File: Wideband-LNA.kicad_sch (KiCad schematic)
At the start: 30 parts, among them J1 RF-IN, J2 RF-OUT, J3 USB_C_Receptacle_USB2.0_16P, U1 TQP3M9036, U2 AP2127K-ADJ

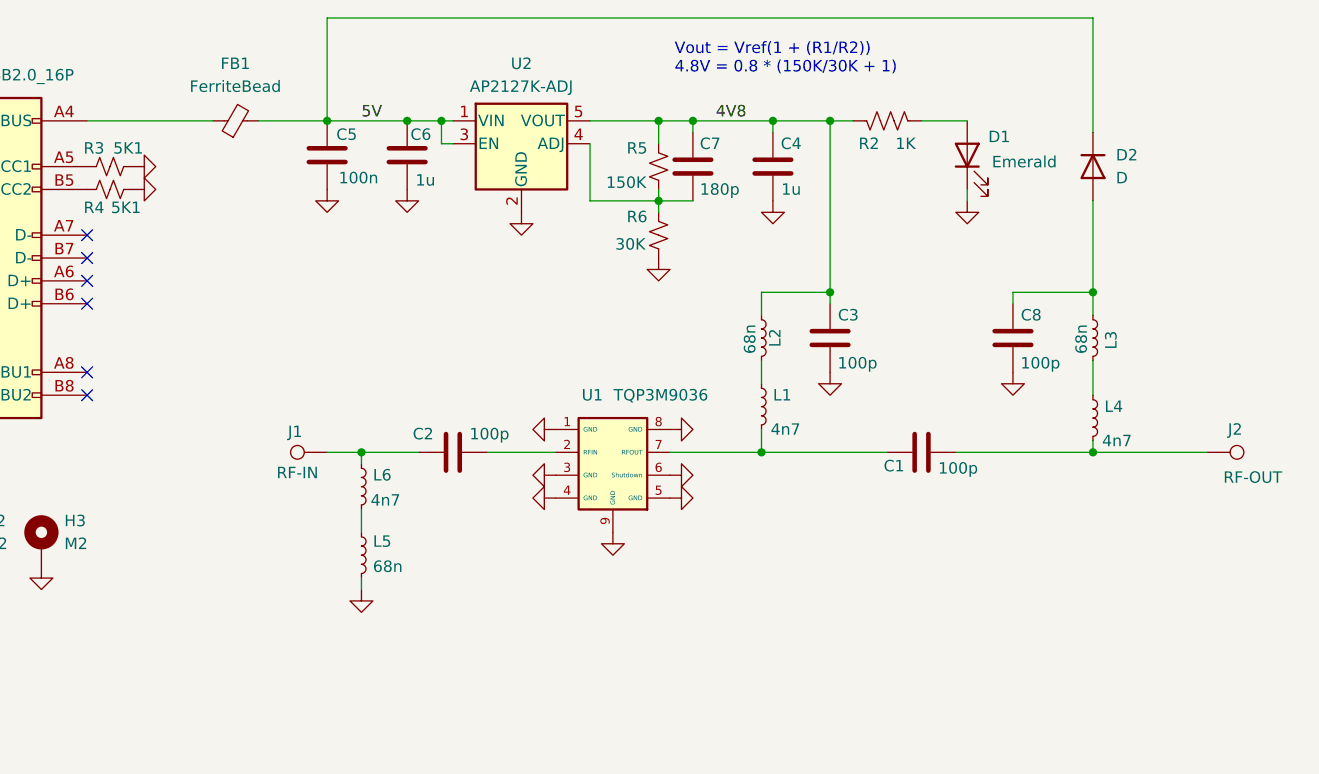
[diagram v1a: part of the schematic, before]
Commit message: updated design to match input at 144 MHz based on uSimmics modeling added 10 ohm resistor in power lead per suggestion from ZMS
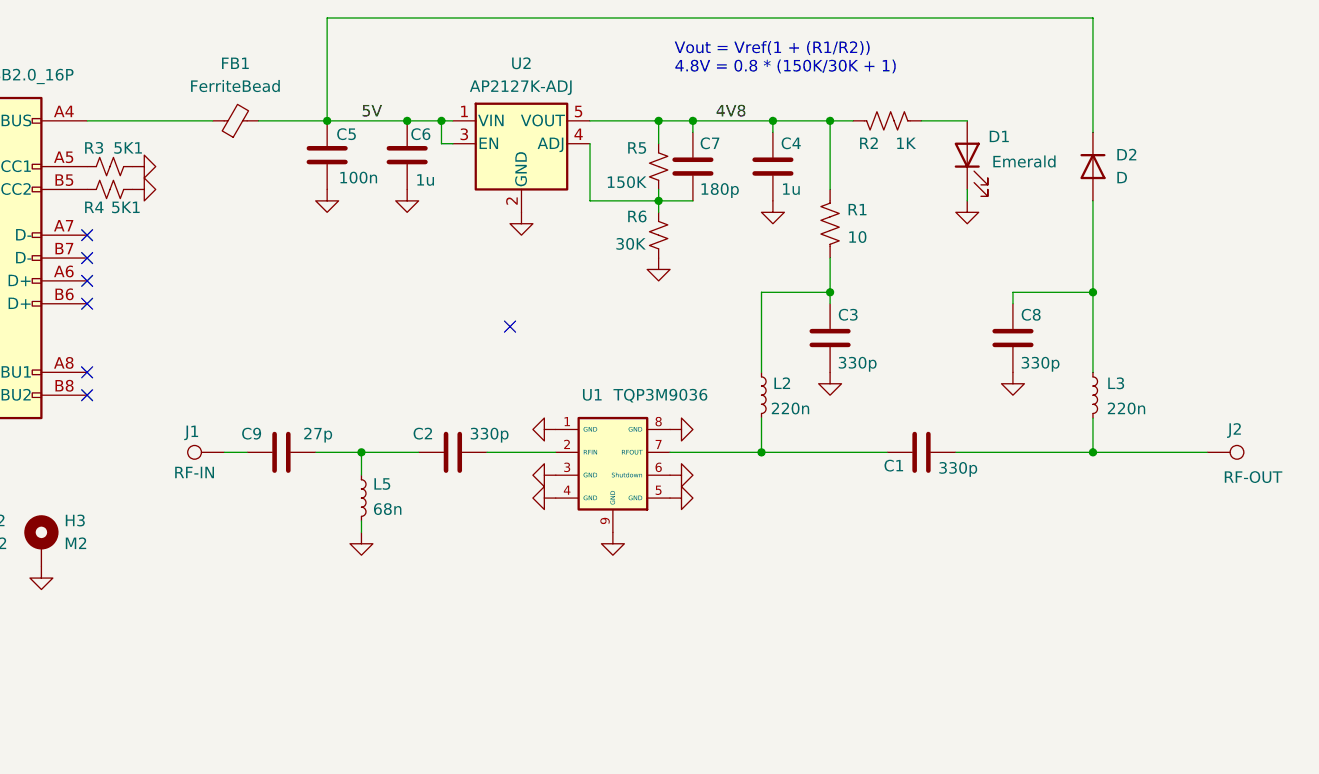
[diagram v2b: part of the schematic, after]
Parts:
- removed L1, L4, L6: 4n7, Inductor_SMD:L_0402_1005Metric, symbol Device:L_Small
- added C9: 27p, Capacitor_SMD:C_0402_1005Metric, symbol Device:C
- added R1: 10, Resistor_SMD:R_0402_1005Metric, symbol Device:R_US
- C1, C2, C3, C8: value 100p -> 330p
- L2, L3: value 68n -> 220n
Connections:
- net 4V8: now also R1.1; no longer C3.1, L2.1
- net at L2.2: now also C1.1, U1.7 (RFOUT)
- net at C1.2, J2.1: now also L3.2
- net at C2.1: now also L5.1, C9.2; no longer J1.1
- new net: C3.1, L2.1, R1.2
- new net: C9.1, J1.1
- no-connect marks 6 -> 7
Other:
- moved on the sheet: J1, L2, L3, L5

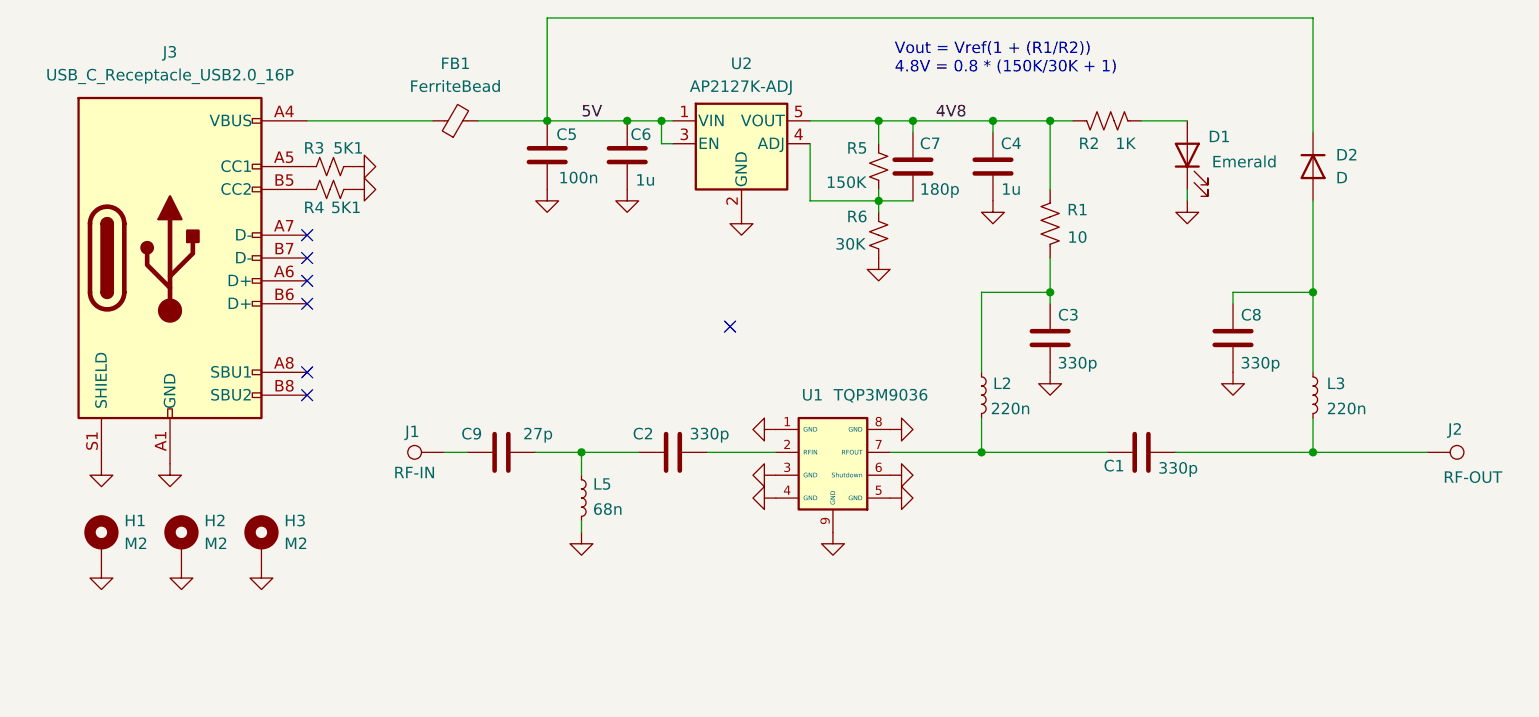
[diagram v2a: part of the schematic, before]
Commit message: Update layout to 19x19 enclosure, TQP3M9036 Improved ground via to isolate voltage regulator circuit from input goal of improving stability Add solder mask relief near output to improve contact with enclosure
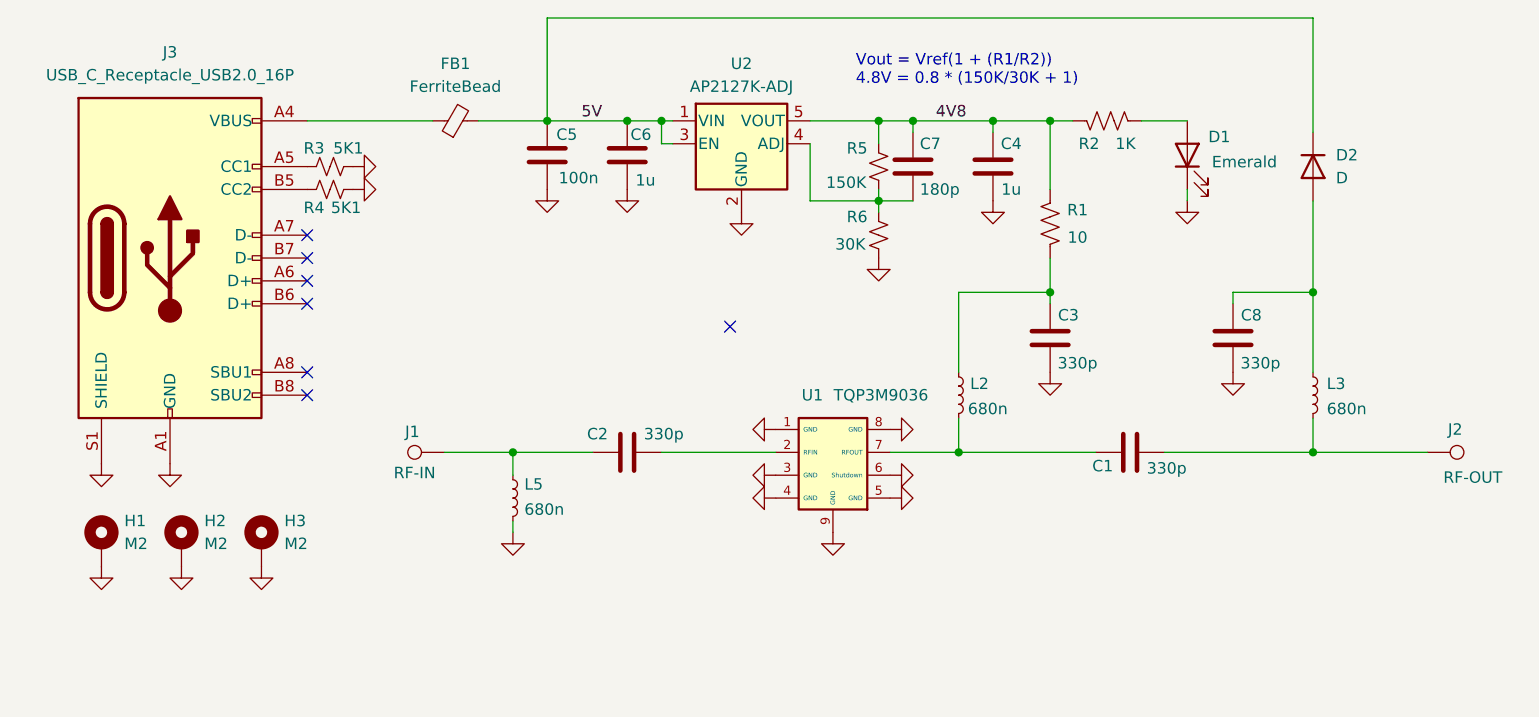
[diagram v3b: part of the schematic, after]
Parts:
- removed C9: 27p, Capacitor_SMD:C_0402_1005Metric, symbol Device:C
- D2: footprint Diode_SMD:D_SOD-123F -> Diode_SMD:D_SOD-523
- L2, L3: value 220n -> 680n
- L5: value 68n -> 680n
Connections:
- net at C2.1, L5.1: now also J1.1
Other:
- moved on the sheet: C1, C2, L2, L5

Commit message: Updated sheet titles to show Version and Git Branch
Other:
- note added: "Git Branch TQP3M9036_19x19_V3.4"
- note added: "November, 2025"
- note added: "Qorvo TQP3M9036 LNA 50 to 1500 MHz"
- note added: "V3.4"
- note removed: "January, 2025"
- note removed: "Qorvo TQP3M9037 LNA 0.5 dB NF, 18 dB gain, 33 dB OIP3, 500 to 6 GHz"
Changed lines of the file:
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@@
 	(generator_version "9.0")
 	(paper "USLetter")
+	(text "Git Branch TQP3M9036_19x19_V3.4"
+		(exclude_from_sim no)
+		(at 209.042 185.928 0)
+		(effects
+			(font
+				(size 1.27 1.27)
+			)
+		)
+	)
 	(text "V1\n"
 		(exclude_from_sim no)
@@
 		)
 	)
-	(text "January, 2025"
+	(text "November, 2025"
 		(exclude_from_sim no)
-		(at 214.122 193.294 0)
+		(at 198.374 199.136 0)
+		(effects
+			(font
+				(size 1.27 1.27)
+			)
+		)
+	)
+	(text "V3.4"
+		(exclude_from_sim no)
+		(at 253.492 199.39 0)
 		(effects
 			(font
@@
 		)
 	)
-	(text "Qorvo TQP3M9037 LNA 0.5 dB NF, 18 dB gain, 33 dB OIP3, 500 to 6 GHz"
+	(text "Qorvo TQP3M9036 LNA 50 to 1500 MHz"
 		(exclude_from_sim no)
-		(at 224.028 189.992 0)
+		(at 189.992 195.58 0)
 		(effects
 			(font

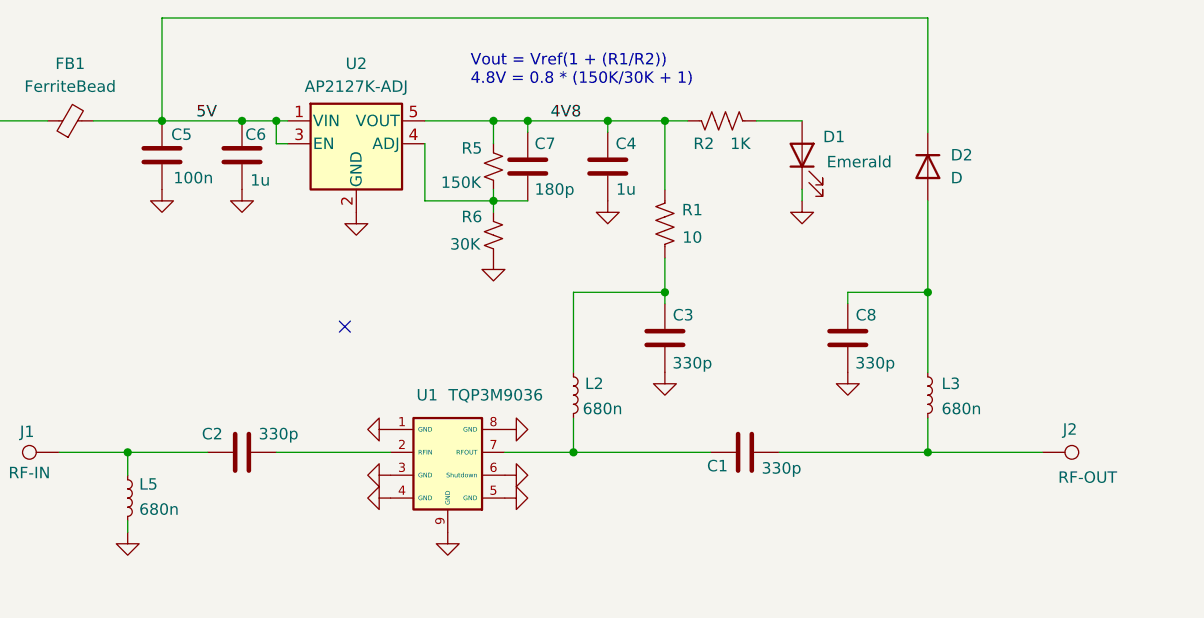
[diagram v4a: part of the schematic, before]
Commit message: Add zone mask to relieve ground plane under component pads
Added screen shot of JLCPCB impedance calculator
Removed bias T components
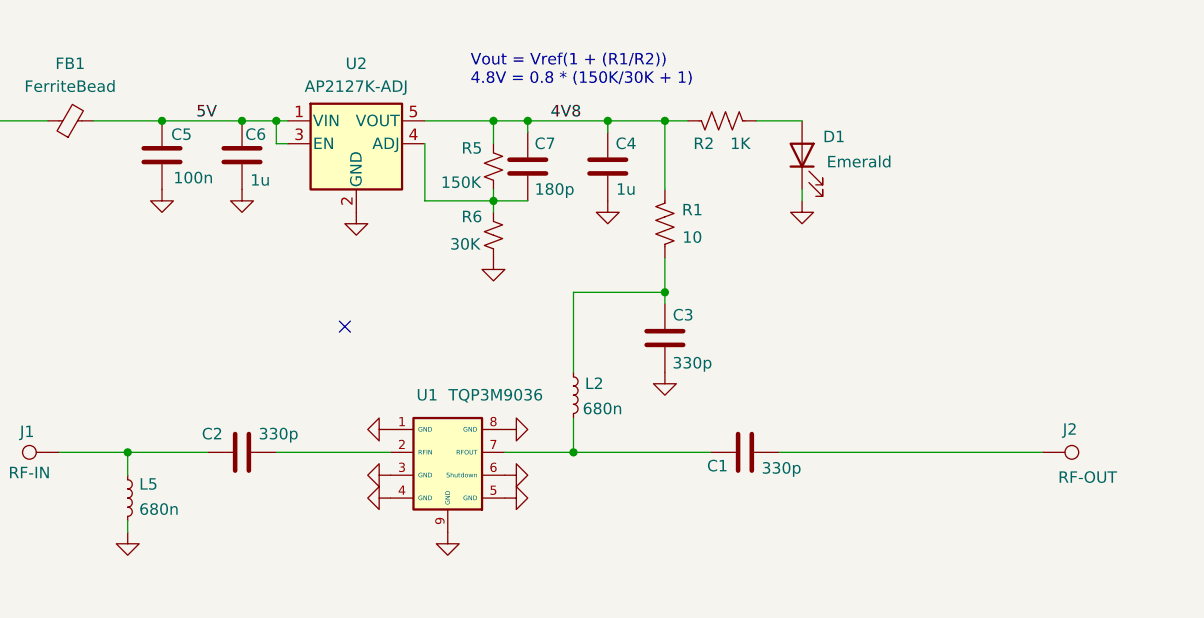
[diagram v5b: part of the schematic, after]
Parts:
- removed C8: 330p, Capacitor_SMD:C_0402_1005Metric, symbol Device:C
- removed D2: D, Diode_SMD:D_SOD-523, symbol Device:D
- removed L3: 680n, Inductor_SMD:L_0603_1608Metric, symbol Device:L_Small

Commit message: Preparing for fab and assy
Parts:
- removed D1: Emerald, Diode_SMD:D_0402_1005Metric, symbol Device:LED
- removed R2: 1K, Resistor_SMD:R_0402_1005Metric, symbol Device:R_US
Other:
- moved on the sheet: C1, C3, C4, C5, C6, C7, L2, R1

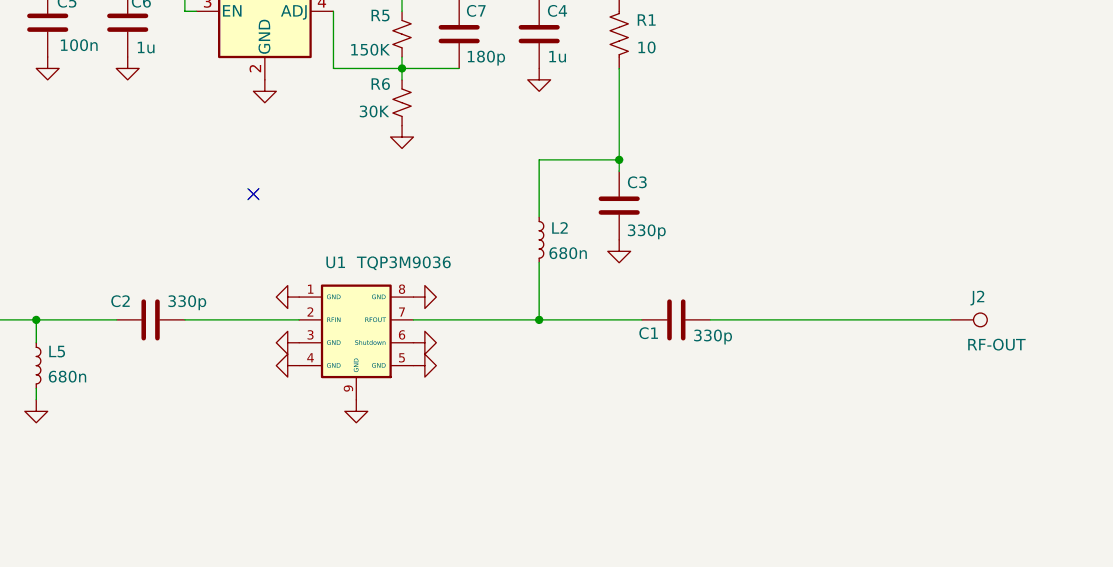
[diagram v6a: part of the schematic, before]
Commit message: Added s2p models, simulated with attenuator and flattened gain simulated  9036 and 9037 updated schematic and layout to remove bias T and LED, prep for attenuator
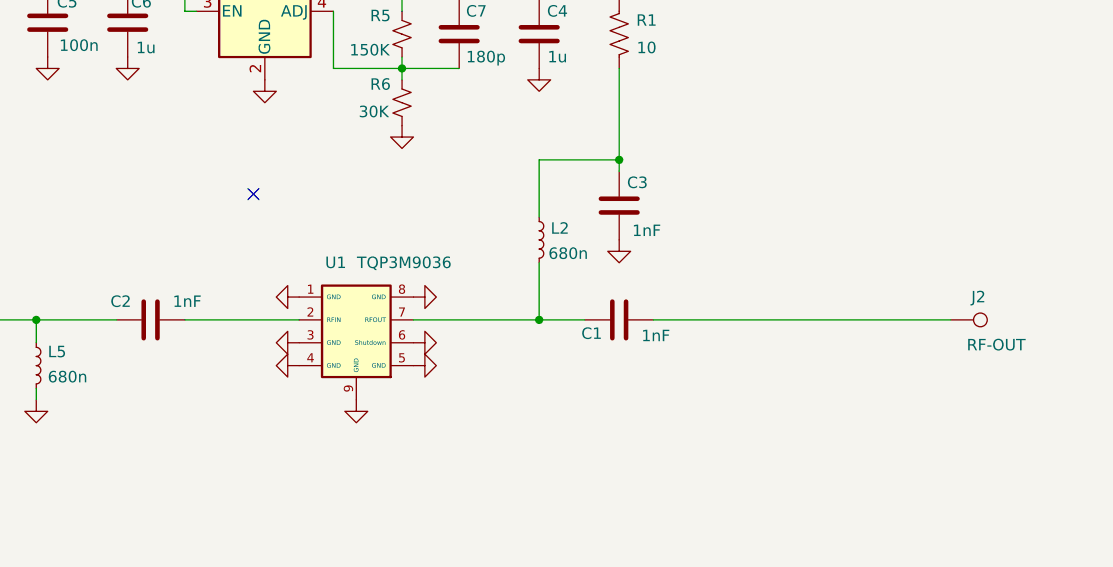
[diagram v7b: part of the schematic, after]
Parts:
- C1, C2, C3: value 330p -> 1nF
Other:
- moved on the sheet: C1
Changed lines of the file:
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@@
 	(wire
 		(pts
-			(xy 177.8 106.68) (xy 189.23 106.68)
+			(xy 177.8 106.68) (xy 182.88 106.68)
 		)
 		(stroke
@@
 	(wire
 		(pts
-			(xy 196.85 106.68) (xy 223.52 106.68)
+			(xy 190.5 106.68) (xy 223.52 106.68)
 		)
 		(stroke
@@
 	(symbol
 		(lib_id "Device:C")
-		(at 193.04 106.68 90)
+		(at 186.69 106.68 90)
 		(unit 1)
 		(exclude_from_sim no)
@@
 		(dnp no)
 		(property "Reference" "C1"
-			(at 189.992 108.204 90)
-			(effects
-				(font
-					(size 1.27 1.27)
-				)
-			)
-		)
-		(property "Value" "330p"
-			(at 197.104 108.458 90)
+			(at 183.642 108.204 90)
+			(effects
+				(font
+					(size 1.27 1.27)
+				)
+			)
+		)
+		(property "Value" "1nF"
+			(at 190.754 108.458 90)
 			(effects
 				(font
@@
 		)
 		(property "Footprint" "Capacitor_SMD:C_0402_1005Metric"
-			(at 196.85 105.7148 0)
+			(at 190.5 105.7148 0)
 			(effects
 				(font
@@
 		)
 		(property "Datasheet" "~"
-			(at 193.04 106.68 0)
+			(at 186.69 106.68 0)
 			(effects
 				(font
@@
 		)
 		(property "Description" "Unpolarized capacitor"
-			(at 193.04 106.68 0)
+			(at 186.69 106.68 0)
 			(effects
 				(font
@@
 		)
 		(property "LCSC" "C1546"
-			(at 189.992 104.648 0)
+			(at 183.642 104.648 0)
 			(effects
 				(font
@@
 			)
 		)
-		(property "Value" "330p"
+		(property "Value" "1nF"
 			(at 138.684 104.648 90)
 			(effects
@@
 			)
 		)
-		(property "Value" "330p"
+		(property "Value" "1nF"
 			(at 189.738 96.774 0)
 			(effects

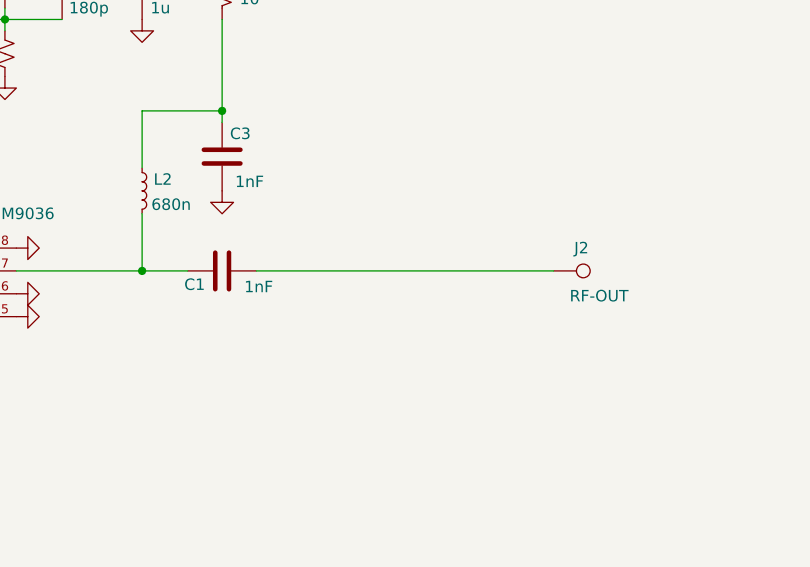
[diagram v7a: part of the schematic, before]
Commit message: Added attenuator with high frequency bypass on output
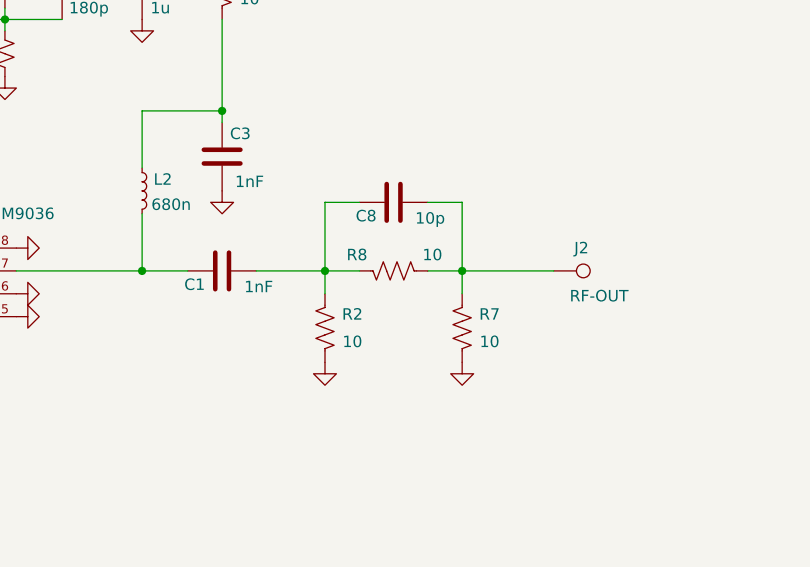
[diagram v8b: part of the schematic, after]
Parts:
- added C8: 10p, Capacitor_SMD:C_0402_1005Metric, symbol Device:C
- added R2, R7, R8: 10, Resistor_SMD:R_0402_1005Metric, symbol Device:R_US
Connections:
- net GND: now also R2.2, R7.2
- net at C1.2: now also C8.1, R2.1, R8.1; no longer J2.1
- new net: C8.2, J2.1, R7.1, R8.2
